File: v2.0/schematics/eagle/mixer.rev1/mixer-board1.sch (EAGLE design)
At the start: 8 parts

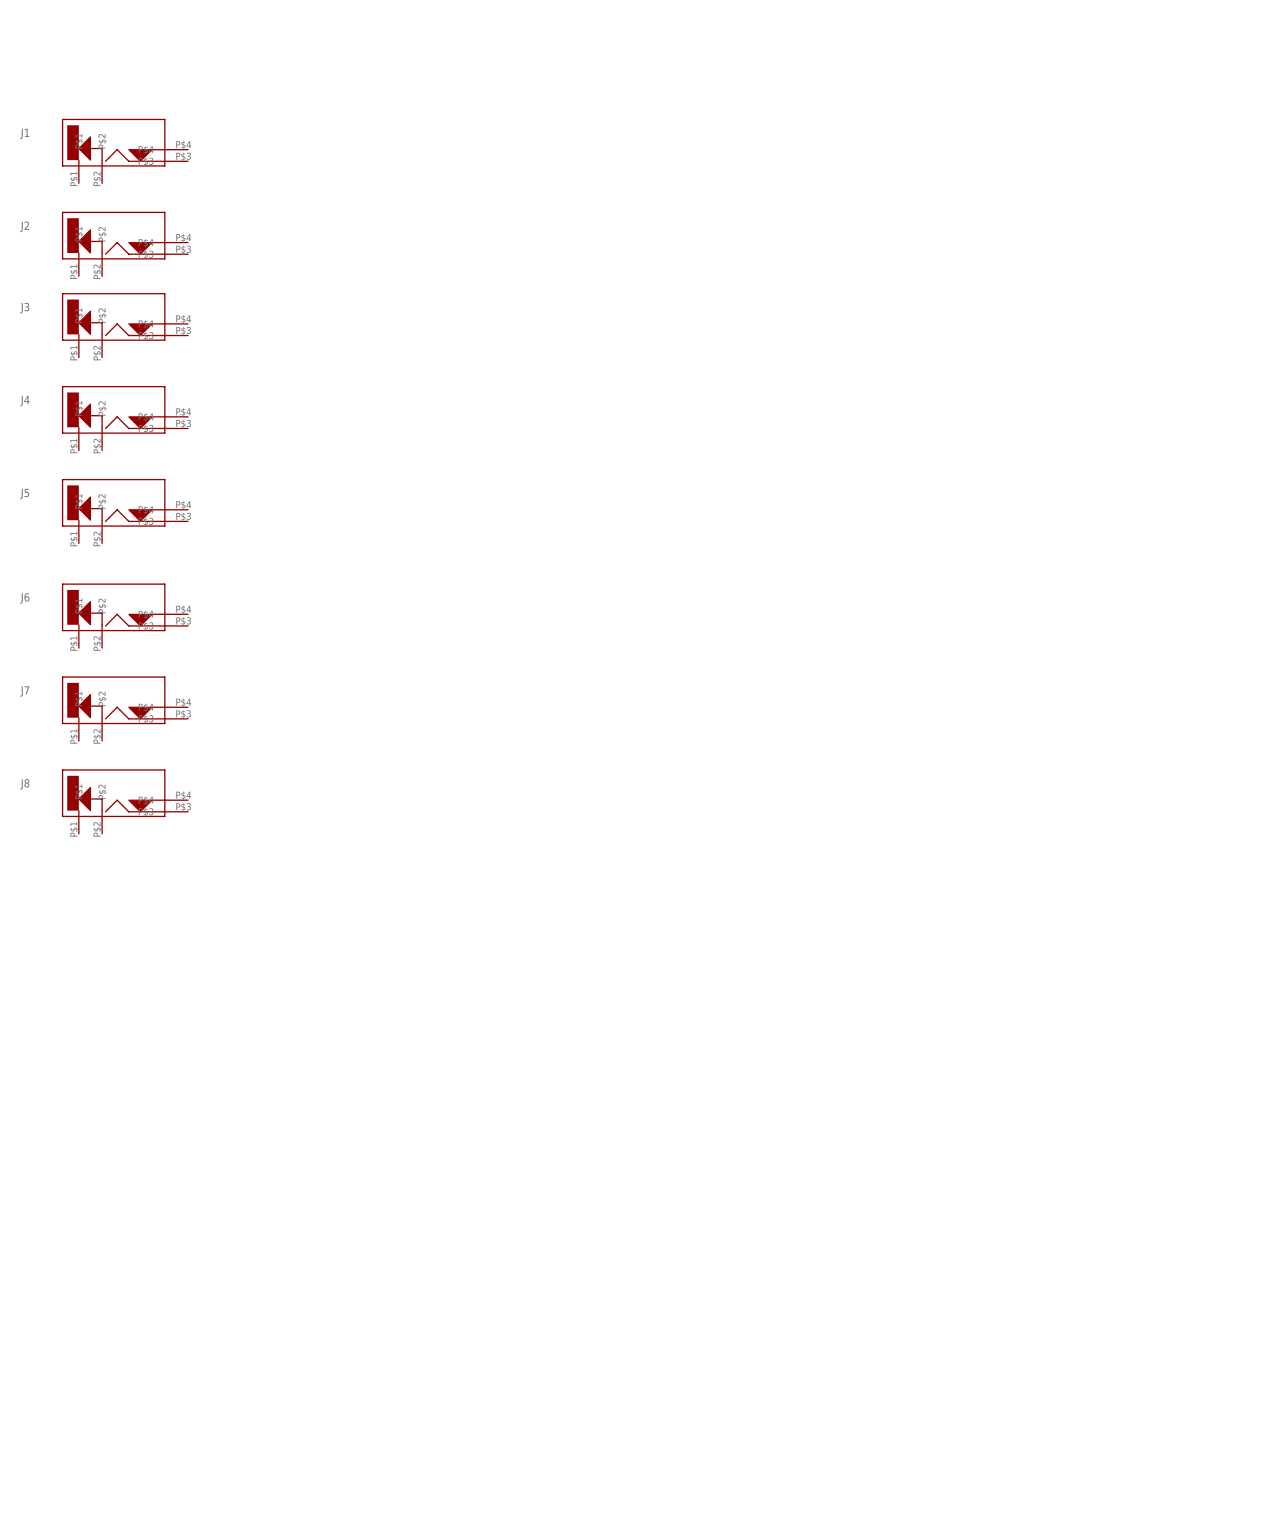
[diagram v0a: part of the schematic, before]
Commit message: Added input stage to mixer
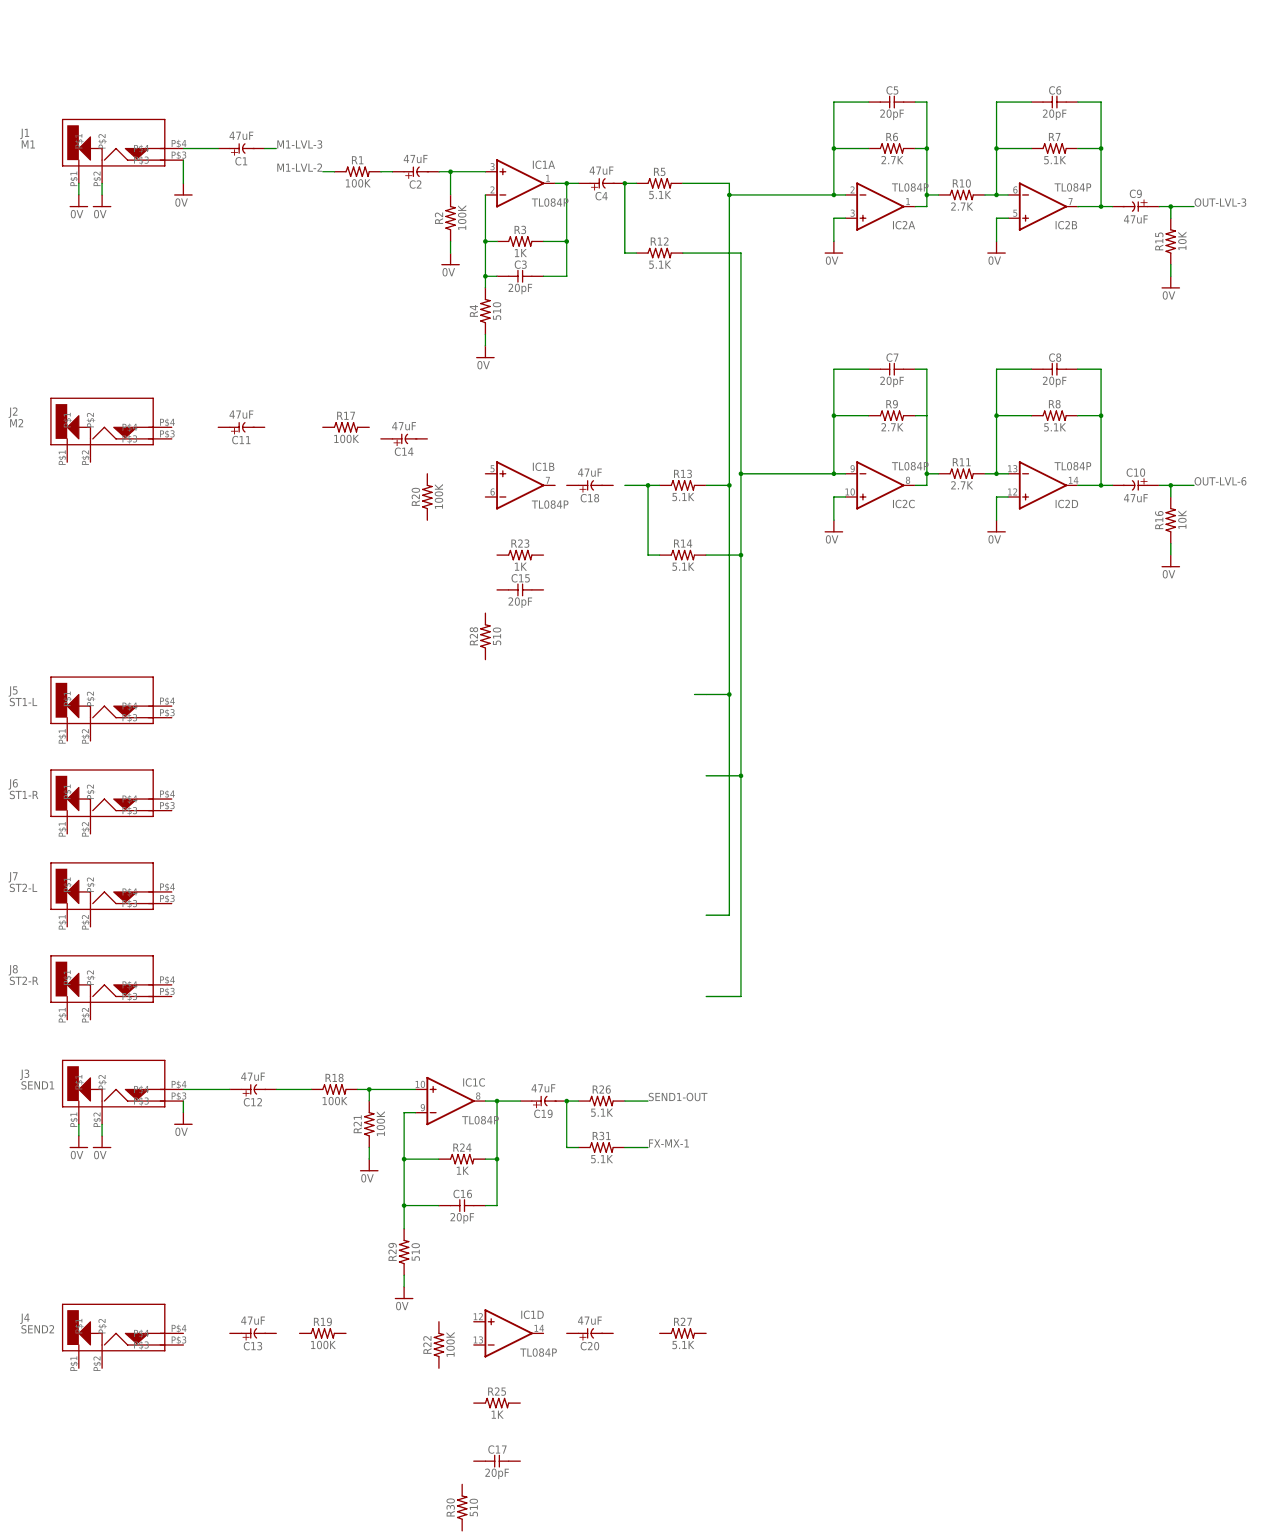
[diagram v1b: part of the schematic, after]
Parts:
- added C1, C10, C11, C12, C13, C14, C18, C19, C2, C20, C4, C9: 47uF, _common:CE-USE2-5
- added C15, C16, C17, C3, C5, C6, C7, C8: 20pF, _common:CC-US025-024X044
- added IC1, IC2: TL084P, _common:TL084P
- added R1, R17, R18, R19, R2, R20, R21, R22: 100K, _common:R
- added R10, R11, R6, R9: 2.7K, _common:R
- added R12, R13, R14, R26, R27, R31, R5, R7, R8: 5.1K, _common:R
- added R15, R16: 10K, _common:R
- added R23, R24, R25, R3: 1K, _common:R
- added R28, R29, R30, R4: 510, _common:R
- J1: value (none) -> M1
- J2: value (none) -> M2
- J3: value (none) -> SEND1
- J4: value (none) -> SEND2
- J5: value (none) -> ST1-L
- J6: value (none) -> ST1-R
- J7: value (none) -> ST2-L
- J8: value (none) -> ST2-R
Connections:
- new net 0V: IC2A.+IN, IC2B.+IN, IC2C.+IN, IC2D.+IN, J1.P$1, J1.P$2, J1.P$3, J3.P$1, J3.P$2, J3.P$3, R15.1, R16.1, R2.1, R21.1, R29.1, R4.1
- new net FX-MX-1: R31.2
- new net M1-LVL-2: R1.1
- new net M1-LVL-3: C1.-
- new net N$1: C1.+, J1.P$4
- new net N$10: R13.1, R14.1
- new net N$11: C7.1, IC2C.OUT, R11.1, R9.2
- new net N$12: C8.2, IC2D.-IN, R11.2, R8.1
- new net N$13: C6.1, C9.-, IC2B.OUT, R7.2
- new net N$14: C12.+, J3.P$4
- new net N$15: C7.2, IC2C.-IN, R12.2, R14.2, R9.1
- new net N$16: C12.-, R18.1
- new net N$17: IC1C.+IN, R18.2, R21.2
- new net N$18: C10.-, C8.1, IC2D.OUT, R8.2
- new net N$19: C16.2, IC1C.-IN, R24.1, R29.2
- new net N$2: C3.2, IC1A.-IN, R3.1, R4.2
- new net N$20: C16.1, C19.+, IC1C.OUT, R24.2
- new net N$21: C19.-, R26.1, R31.1
- new net N$3: C2.-, IC1A.+IN, R2.2
- new net N$4: C2.+, R1.2
- new net N$5: C3.1, C4.+, IC1A.OUT, R3.2
- new net N$6: C4.-, R12.1, R5.1
- new net N$7: C5.2, IC2A.-IN, R13.2, R5.2, R6.1
- new net N$8: C5.1, IC2A.OUT, R10.1, R6.2
- new net N$9: C6.2, IC2B.-IN, R10.2, R7.1
- new net OUT-LVL-3: C9.+, R15.2
- new net OUT-LVL-6: C10.+, R16.2
- new net SEND1-OUT: R26.2
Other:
- moved on the sheet: J1, J2, J3, J4, J5, J6, J7, J8

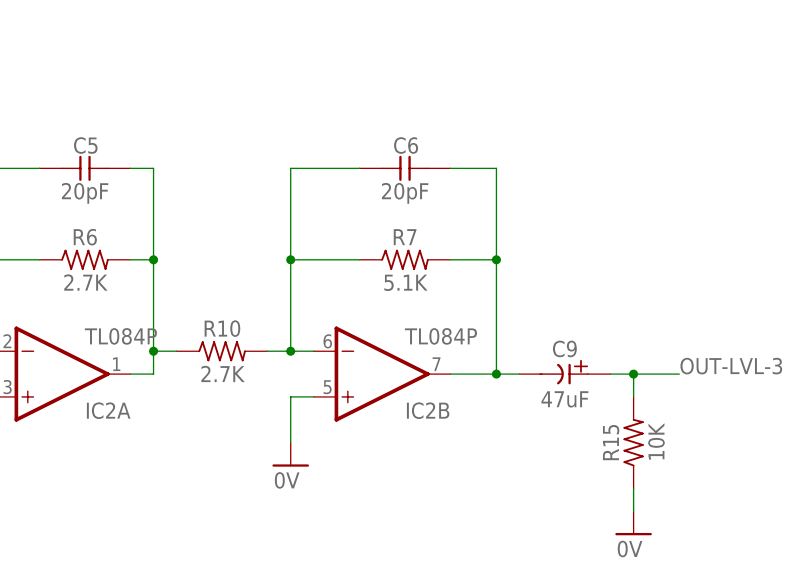
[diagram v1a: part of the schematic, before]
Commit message: Update final amp stage value to line level
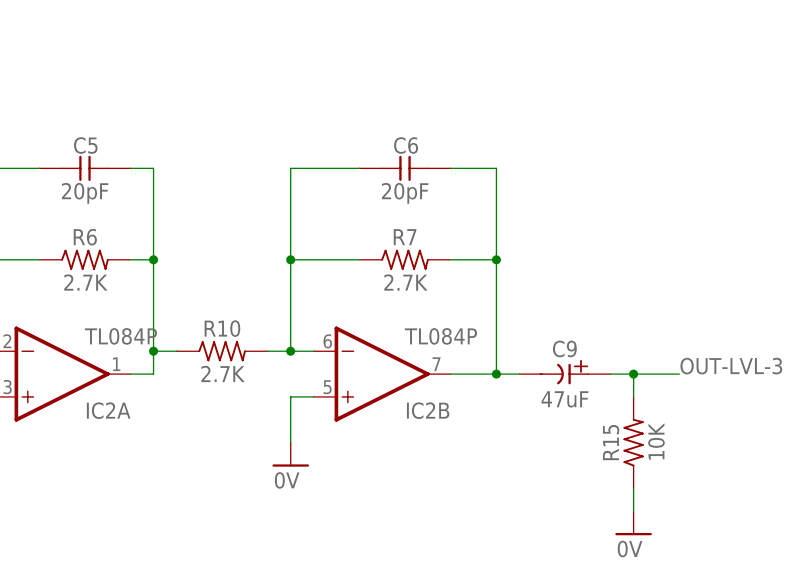
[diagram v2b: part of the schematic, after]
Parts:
- R7: value 5.1K -> 2.7K
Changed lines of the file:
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@@
 <part name="IC2" library="_common" deviceset="TL084" device="P"/>
 <part name="R6" library="_common" deviceset="R" device="" value="2.7K"/>
-<part name="R7" library="_common" deviceset="R" device="" value="5.1K"/>
+<part name="R7" library="_common" deviceset="R" device="" value="2.7K"/>
 <part name="R8" library="_common" deviceset="R" device="" value="5.1K"/>
 <part name="R9" library="_common" deviceset="R" device="" value="2.7K"/>

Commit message: Updated caps to 100uF
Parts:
- C1, C10, C11, C12, C13, C14, C18, C19, C2, C20, C4, C9: value 47uF -> 100uF
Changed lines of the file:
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@@
 <part name="J7" library="jacks" deviceset="CL1384" device="" value="ST2-L"/>
 <part name="J8" library="jacks" deviceset="CL1384" device="" value="ST2-R"/>
-<part name="C1" library="_common" deviceset="CE-US" device="E2-5" value="47uF"/>
+<part name="C1" library="_common" deviceset="CE-US" device="E2-5" value="100uF"/>
 <part name="R1" library="_common" deviceset="R" device="" value="100K"/>
 <part name="GND1" library="supply1" library_urn="urn:adsk.eagle:library:371" deviceset="0V" device=""/>
@@
 <part name="IC1" library="_common" deviceset="TL084" device="P"/>
 <part name="R2" library="_common" deviceset="R" device="" value="100K"/>
-<part name="C2" library="_common" deviceset="CE-US" device="E2-5" value="47uF"/>
+<part name="C2" library="_common" deviceset="CE-US" device="E2-5" value="100uF"/>
 <part name="GND3" library="supply1" library_urn="urn:adsk.eagle:library:371" deviceset="0V" device=""/>
 <part name="R3" library="_common" deviceset="R" device="" value="1K"/>
@@
 <part name="R4" library="_common" deviceset="R" device="" value="510"/>
 <part name="GND4" library="supply1" library_urn="urn:adsk.eagle:library:371" deviceset="0V" device=""/>
-<part name="C4" library="_common" deviceset="CE-US" device="E2-5" value="47uF"/>
+<part name="C4" library="_common" deviceset="CE-US" device="E2-5" value="100uF"/>
 <part name="R5" library="_common" deviceset="R" device="" value="5.1K"/>
 <part name="IC2" library="_common" deviceset="TL084" device="P"/>
@@
 <part name="R13" library="_common" deviceset="R" device="" value="5.1K"/>
 <part name="R14" library="_common" deviceset="R" device="" value="5.1K"/>
-<part name="C9" library="_common" deviceset="CE-US" device="E2-5" value="47uF"/>
-<part name="C10" library="_common" deviceset="CE-US" device="E2-5" value="47uF"/>
+<part name="C9" library="_common" deviceset="CE-US" device="E2-5" value="100uF"/>
+<part name="C10" library="_common" deviceset="CE-US" device="E2-5" value="100uF"/>
 <part name="R15" library="_common" deviceset="R" device="" value="10K"/>
 <part name="R16" library="_common" deviceset="R" device="" value="10K"/>
 <part name="GND9" library="supply1" library_urn="urn:adsk.eagle:library:371" deviceset="0V" device=""/>
 <part name="GND10" library="supply1" library_urn="urn:adsk.eagle:library:371" deviceset="0V" device=""/>
-<part name="C11" library="_common" deviceset="CE-US" device="E2-5" value="47uF"/>
-<part name="C12" library="_common" deviceset="CE-US" device="E2-5" value="47uF"/>
-<part name="C13" library="_common" deviceset="CE-US" device="E2-5" value="47uF"/>
+<part name="C11" library="_common" deviceset="CE-US" device="E2-5" value="100uF"/>
+<part name="C12" library="_common" deviceset="CE-US" device="E2-5" value="100uF"/>
+<part name="C13" library="_common" deviceset="CE-US" device="E2-5" value="100uF"/>
 <part name="R17" library="_common" deviceset="R" device="" value="100K"/>
 <part name="R18" library="_common" deviceset="R" device="" value="100K"/>
@@
 <part name="R21" library="_common" deviceset="R" device="" value="100K"/>
 <part name="R22" library="_common" deviceset="R" device="" value="100K"/>
-<part name="C14" library="_common" deviceset="CE-US" device="E2-5" value="47uF"/>
+<part name="C14" library="_common" deviceset="CE-US" device="E2-5" value="100uF"/>
 <part name="R23" library="_common" deviceset="R" device="" value="1K"/>
 <part name="R24" library="_common" deviceset="R" device="" value="1K"/>
@@
 <part name="C16" library="_common" deviceset="CC-US" device="025-024X044" value="20pF"/>
 <part name="C17" library="_common" deviceset="CC-US" device="025-024X044" value="20pF"/>
-<part name="C18" library="_common" deviceset="CE-US" device="E2-5" value="47uF"/>
-<part name="C19" library="_common" deviceset="CE-US" device="E2-5" value="47uF"/>
-<part name="C20" library="_common" deviceset="CE-US" device="E2-5" value="47uF"/>
+<part name="C18" library="_common" deviceset="CE-US" device="E2-5" value="100uF"/>
+<part name="C19" library="_common" deviceset="CE-US" device="E2-5" value="100uF"/>
+<part name="C20" library="_common" deviceset="CE-US" device="E2-5" value="100uF"/>
 <part name="R26" library="_common" deviceset="R" device="" value="5.1K"/>
 <part name="R27" library="_common" deviceset="R" device="" value="5.1K"/>

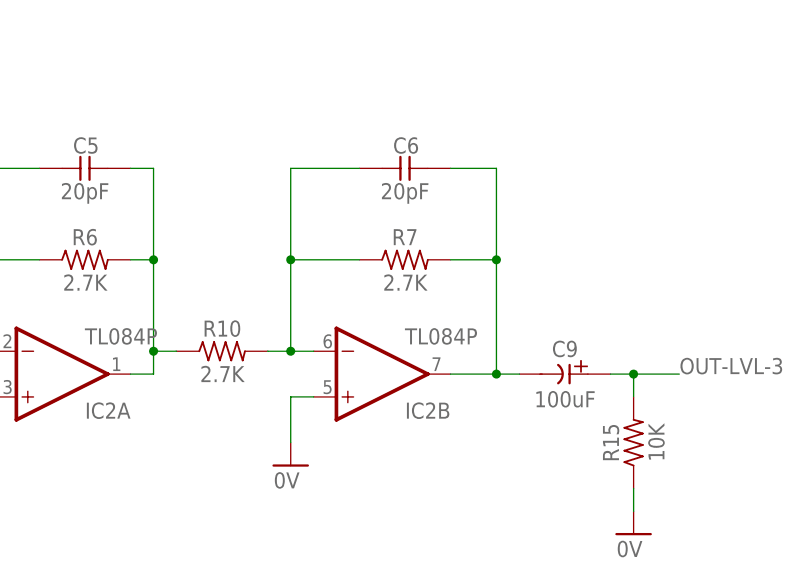
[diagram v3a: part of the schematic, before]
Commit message: Added stereo line in; output level
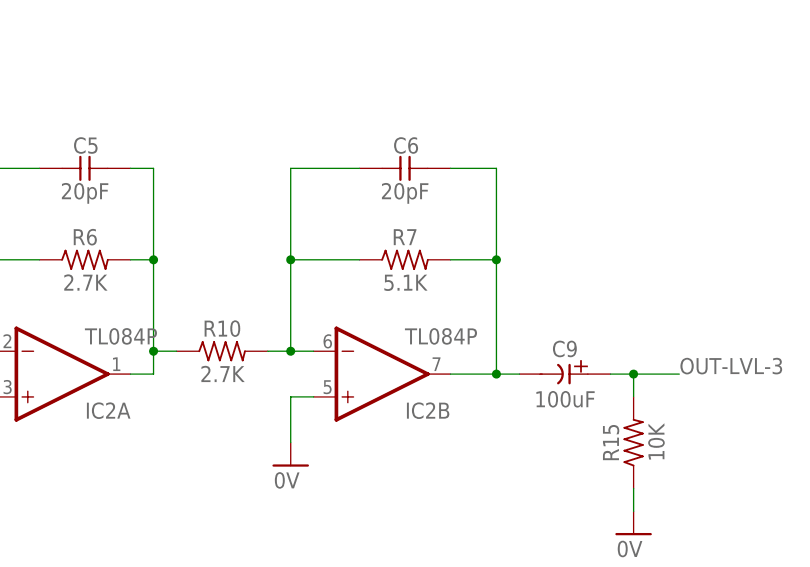
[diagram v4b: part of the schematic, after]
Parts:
- R7: value 2.7K -> 5.1K
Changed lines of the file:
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@@
 <part name="IC2" library="_common" deviceset="TL084" device="P"/>
 <part name="R6" library="_common" deviceset="R" device="" value="2.7K"/>
-<part name="R7" library="_common" deviceset="R" device="" value="2.7K"/>
+<part name="R7" library="_common" deviceset="R" device="" value="5.1K"/>
 <part name="R8" library="_common" deviceset="R" device="" value="5.1K"/>
 <part name="R9" library="_common" deviceset="R" device="" value="2.7K"/>
